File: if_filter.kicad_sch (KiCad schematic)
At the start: 10 parts, among them Y1 9MHz, Y2 9MHz, Y3 9MHz, Y4 9MHz

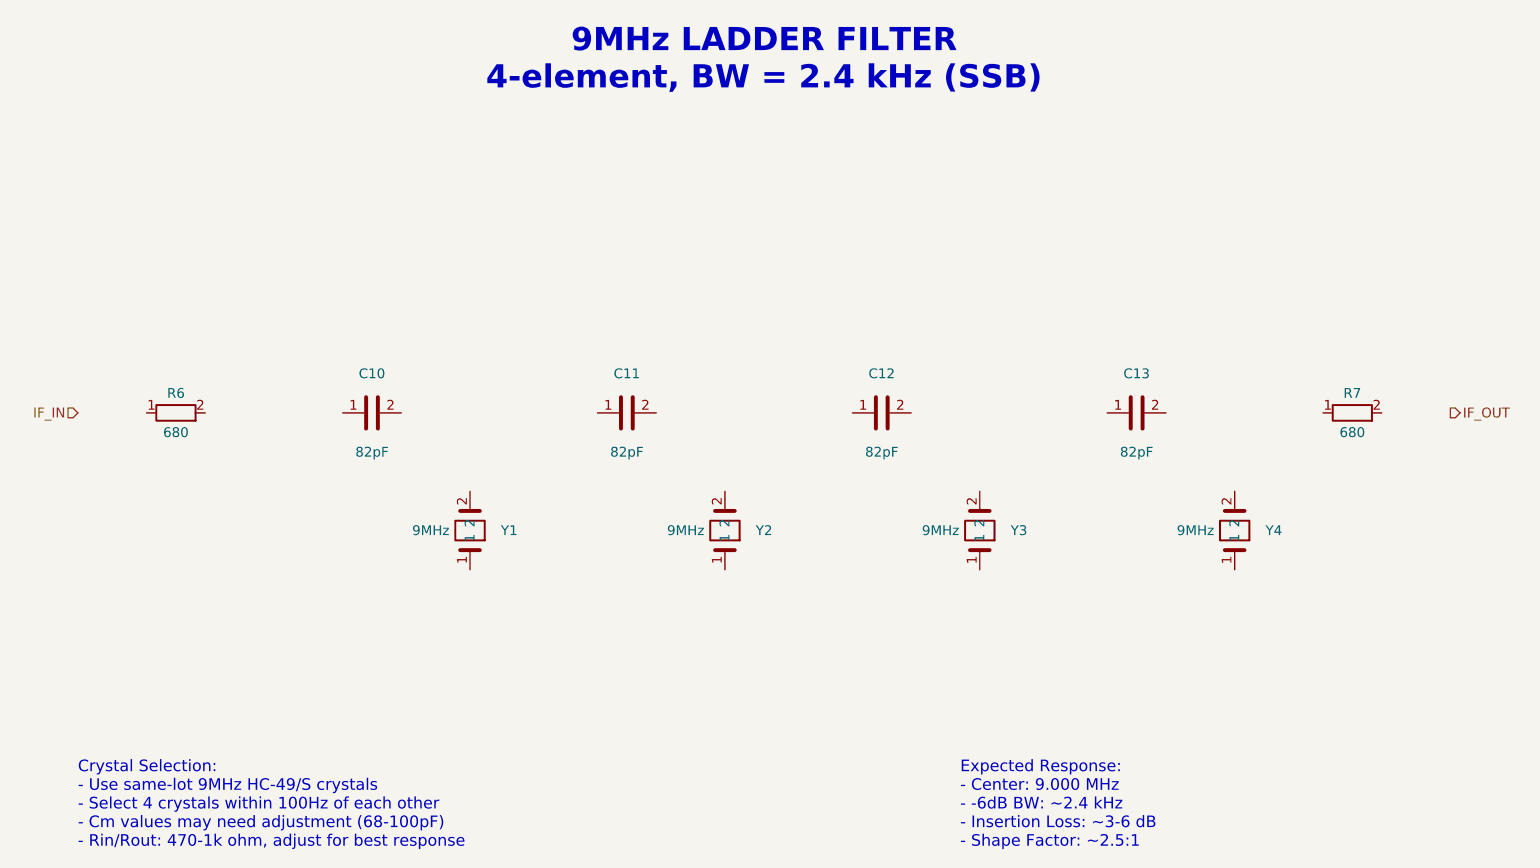
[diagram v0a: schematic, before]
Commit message: Add initial PCB layout with complete component placement
- Create 2-layer PCB (200x100mm) based on KiCad schematic import
- Place all components including Arduino Nano, Si5351, SA612 mixers, SSD1306 OLED
- Position audio amplifier (LM386), voltage regulators (7805/7808), crystal filters
- Add discrete components: resistors, capacitors, inductors, diodes, transistors
- Include connectors for power (DC jack), antenna, speaker, and microphone
- Update .gitignore to exclude fp-info-cache and backup directories
- Update schematic symbols for all circuit blocks (audio, BPF/LPF, control, IF filter, mixer/modulator, power amp, power supply)
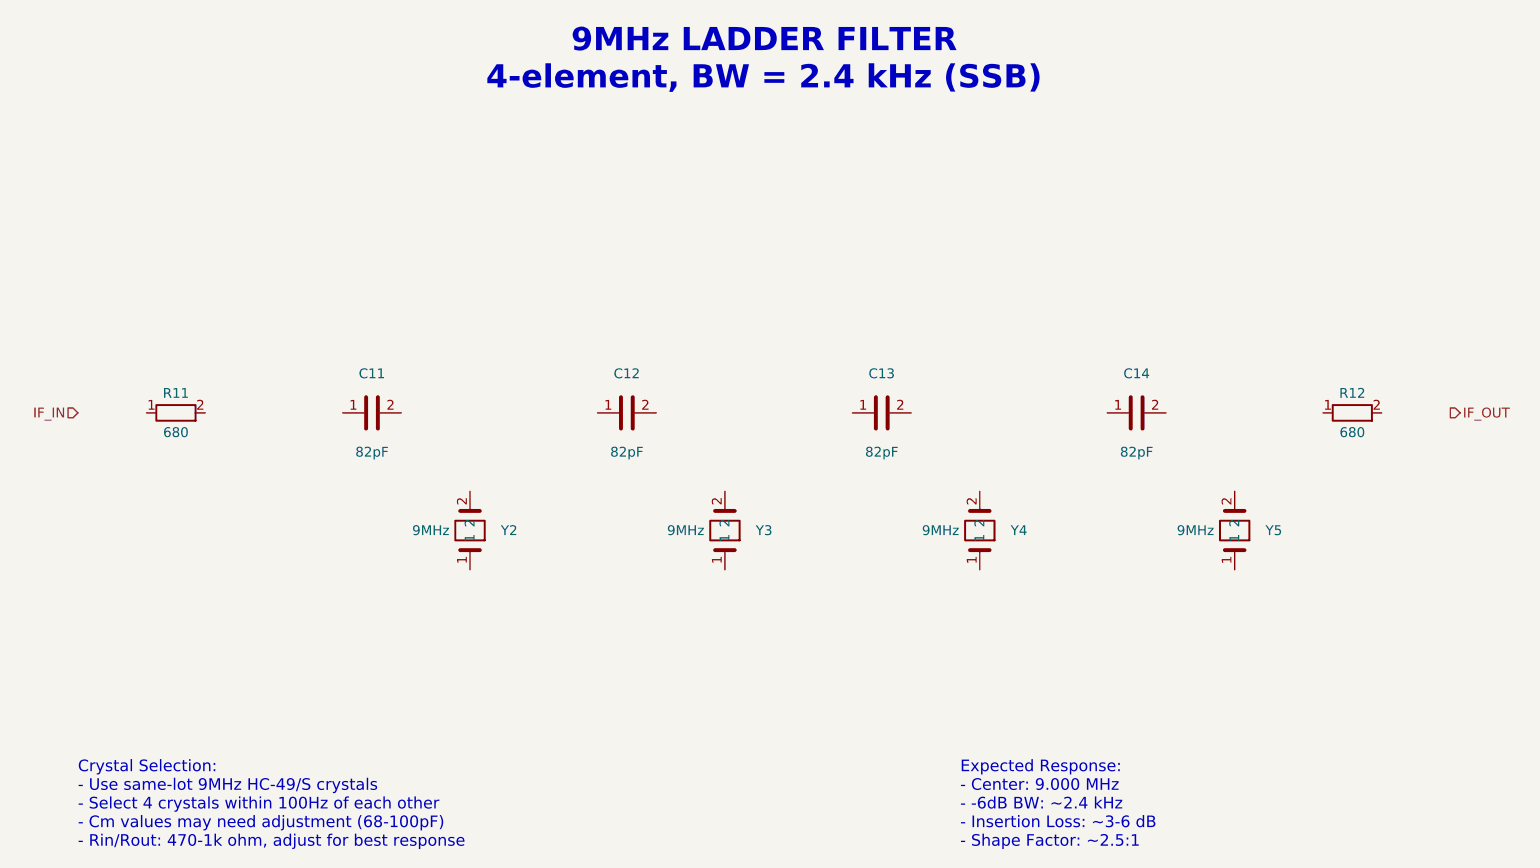
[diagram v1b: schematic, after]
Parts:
- removed C10: 82pF, symbol Device:C
- removed R6, R7: 680, symbol Device:R
- removed Y1: 9MHz, symbol Crystal:Crystal
- added C14: 82pF, Capacitor_THT:C_Disc_D5.0mm_W2.5mm_P5.00mm, symbol Device:C
- added R11, R12: 680, Resistor_THT:R_Axial_DIN0207_L6.3mm_D2.5mm_P10.16mm_Horizontal, symbol Device:R
- added Y5: 9MHz, Crystal:Crystal_HC49-4H_Vertical, symbol Crystal:Crystal
- C11, C12, C13: footprint (none) -> Capacitor_THT:C_Disc_D5.0mm_W2.5mm_P5.00mm
- Y2, Y3, Y4: footprint (none) -> Crystal:Crystal_HC49-4H_Vertical
